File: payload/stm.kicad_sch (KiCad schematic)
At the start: 17 parts, among them J401 Conn_01x06_Female, U401 STM32F103C8T6, Y401 8MHz

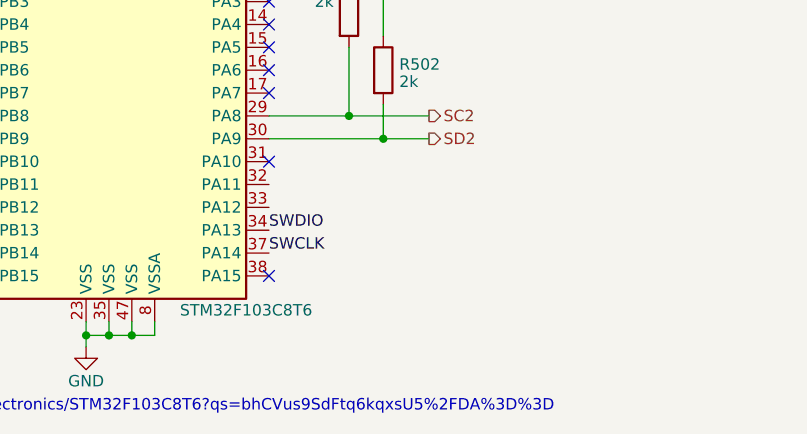
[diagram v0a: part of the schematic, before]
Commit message: added LEDs
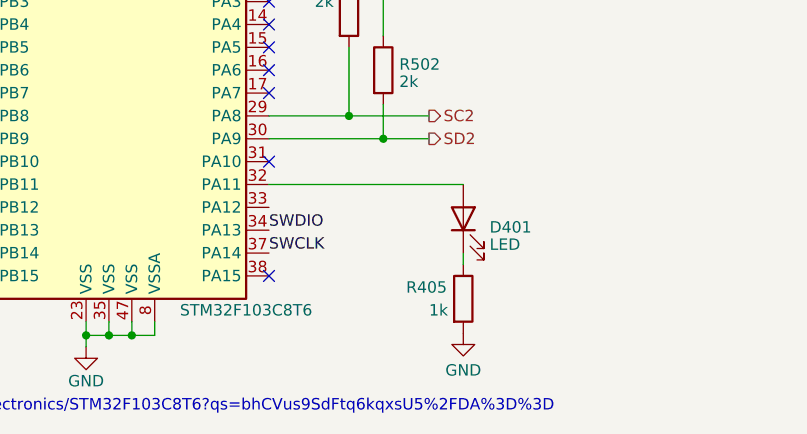
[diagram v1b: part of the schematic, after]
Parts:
- added D401: LED, LED_SMD:LED_0402_1005Metric_Pad0.77x0.64mm_HandSolder, symbol Device:LED
- added R405: 1k, Capacitor_SMD:C_0603_1608Metric_Pad1.08x0.95mm_HandSolder, symbol Device:R
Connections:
- net GND: now also R405.2
- net at U401.32 (PA11): now also D401.2 (A)
- new net: D401.1 (K), R405.1
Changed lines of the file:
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@@
+    (stroke (width 0) (type default))
+  )
+  (wire (pts (xy 186.69 140.97) (xy 186.69 142.24))
+    (stroke (width 0) (type default))
+  )
+  (wire (pts (xy 165.1 133.35) (xy 186.69 133.35))
     (stroke (width 0) (type default))
   )
@@
     (effects (font (size 1.27 1.27)) (justify left))
   )
+  (symbol (lib_id "Device:LED") (at 186.69 137.16 90) (unit 1)
+    (in_bom yes) (on_board yes) (dnp no) (fields_autoplaced)
+    (property "Reference" "D401" (at 189.611 138.1038 90)
+      (effects (font (size 1.27 1.27)) (justify right))
+    )
+    (property "Value" "LED" (at 189.611 140.0248 90)
+      (effects (font (size 1.27 1.27)) (justify right))
+    )
+    (property "Footprint" "LED_SMD:LED_0402_1005Metric_Pad0.77x0.64mm_HandSolder" (at 186.69 137.16 0)
+      (effects (font (size 1.27 1.27)) hide)
+    )
+    (property "Datasheet" "~" (at 186.69 137.16 0)
+      (effects (font (size 1.27 1.27)) hide)
+    )
+    (pin "1")
+    (pin "2")
+    (instances
+      (project "payload"
+        (path "/0a419cb9-bfa0-442e-8f67-9cc2093d7c87/dea4f99a-06bc-4245-ba10-4d6e21532046"
+          (reference "D401") (unit 1)
+        )
+        (path "/0a419cb9-bfa0-442e-8f67-9cc2093d7c87/49443efe-460a-43e1-9eab-5b039ce0b5ad"
+          (reference "D301") (unit 1)
+        )
+      )
+    )
+  )
   (symbol (lib_id "power:GND") (at 115.57 104.394 0) (unit 1)
     (in_bom yes) (on_board yes) (dnp no)
@@
         (path "/298cdb24-bdd2-4280-a247-0c70bae2ee1c"
           (reference "#PWR0124") (unit 1)
+        )
+      )
+    )
+  )
+  (symbol (lib_id "Device:R") (at 186.69 146.05 0) (unit 1)
+    (in_bom yes) (on_board yes) (dnp no)
+    (property "Reference" "R405" (at 180.34 144.78 0)
+      (effects (font (size 1.27 1.27)) (justify left))
+    )
+    (property "Value" "1k" (at 182.88 147.32 0)
+      (effects (font (size 1.27 1.27)) (justify left))
+    )
+    (property "Footprint" "Capacitor_SMD:C_0603_1608Metric_Pad1.08x0.95mm_HandSolder" (at 184.912 146.05 90)
+      (effects (font (size 1.27 1.27)) hide)
+    )
+    (property "Datasheet" "~" (at 186.69 146.05 0)
+      (effects (font (size 1.27 1.27)) hide)
+    )
+    (pin "1")
+    (pin "2")
+    (instances
+      (project "payload"
+        (path "/0a419cb9-bfa0-442e-8f67-9cc2093d7c87/dea4f99a-06bc-4245-ba10-4d6e21532046"
+          (reference "R405") (unit 1)
+        )
+        (path "/0a419cb9-bfa0-442e-8f67-9cc2093d7c87"
+          (reference "R101") (unit 1)
+        )
+        (path "/0a419cb9-bfa0-442e-8f67-9cc2093d7c87/49443efe-460a-43e1-9eab-5b039ce0b5ad"
+          (reference "R303") (unit 1)
+        )
+      )
+      (project "electrical-power-system"
+        (path "/5987de0a-a772-40e3-9e89-af52950d87bb/a29c39c3-f61d-41a4-b663-9cd24fc958f0"
+          (reference "R401") (unit 1)
         )
       )
@@
         )
       )
+    )
+  )
+  (symbol (lib_id "power:GND") (at 186.69 149.86 0) (unit 1)
+    (in_bom yes) (on_board yes) (dnp no) (fields_autoplaced)
+    (property "Reference" "#PWR0416" (at 186.69 156.21 0)
+      (effects (font (size 1.27 1.27)) hide)
+    )
+    (property "Value" "GND" (at 186.69 153.9955 0)
+      (effects (font (size 1.27 1.27)))
+    )
+    (property "Footprint" "" (at 186.69 149.86 0)
+      (effects (font (size 1.27 1.27)) hide)
+    )
+    (property "Datasheet" "" (at 186.69 149.86 0)
+      (effects (font (size 1.27 1.27)) hide)
+    )
+    (pin "1")
+    (instances
+      (project "payload"
+        (path "/0a419cb9-bfa0-442e-8f67-9cc2093d7c87/dea4f99a-06bc-4245-ba10-4d6e21532046"
+          (reference "#PWR0416") (unit 1)
+        )
+        (path "/0a419cb9-bfa0-442e-8f67-9cc2093d7c87/49443efe-460a-43e1-9eab-5b039ce0b5ad"
+          (reference "#PWR0309") (unit 1)
+        )
+      )
+      (project "electrical-power-system"
+        (path "/5987de0a-a772-40e3-9e89-af52950d87bb/a29c39c3-f61d-41a4-b663-9cd24fc958f0"
+          (reference "#PWR0408") (unit 1)
+        )
+      )
